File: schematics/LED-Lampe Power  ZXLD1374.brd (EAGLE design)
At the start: 100 x 51.4 mm, 50 parts, among them X2 MKDSN1,5/4-5,08, X6 MKDSN1,5/2-5,08

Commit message: - finalized layout - moved to eagle 6.5
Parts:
- added C25: 220µF / 50V Pan FR, rcl:E5-10,5
- C1: value 470µ / 50V -> 220µF / 50V Pan FR; device rcl:E5-13 -> rcl:E5-10,5
- R25, R3, R9: device resistor:R1206 -> rcl:R1206
- R7, R8: device resistor:R1206@1 -> rcl:R1206
- U$1: value FASTON_PIS4728 220µH -> PIS4728 220µH
- U$2, U$3: value FASTON_PIS4728 100µH -> PIS4728 100µH
- moved C1 17.3 mm to (58.4, 19.8), turned to 270 degrees
- moved C19 15.8 mm to (43.5, 20.0), flipped to the top, turned to 0 degrees
- moved R25 15.3 mm to (40.3, 18.6), flipped to the top, turned to 90 degrees
- moved C20 10.8 mm to (43.5, 17.1), flipped to the top, turned to 0 degrees
- moved C35 4.27 mm to (54.5, 17.1), turned to 0 degrees
- moved C24 4.02 mm to (54.5, 20.0), turned to 0 degrees
- moved R7 3.90 mm to (51.1, 18.6), turned to 90 degrees
- moved C11 2.70 mm to (35.7, 33.2), flipped to the bottom
- moved C2 1.11 mm to (32.9, 22.9)
- moved C32 1.11 mm to (32.9, 19.7)
- moved R3 1.11 mm to (36.0, 21.3)
- moved C13 0.48 mm to (22.4, 33.7)
- moved C6 0.16 mm to (24.6, 32.4)
- moved U$5 0.05 mm to (62.5, 42.5)
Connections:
- net +24V: no longer C1.+
- net GND: now also C25.-
- net N$48: now also C25.+
- net N$7: now also C1.+
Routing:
- net N$48: track 9.02 -> 22.8 mm
- net N$6: track 91.0 -> 81.8 mm
- net +24V: track 53.3 -> 45.7 mm
- net N$7: track 17.3 -> 21.1 mm
- net N$12: track 51.5 -> 49.2 mm
- net N$1: track 26.6 -> 24.3 mm

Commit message: - fix ZXLD1374 case
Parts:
- removed U$1: PIS4728 220µH, LED-Treiber:FASTON_PIS4728
- removed U$2: PIS4728 100µH, LED-Treiber:FASTON_PIS4728
- added L$1: PIS4728 220µH, LED-Treiber:FASTON_PIS4728
- added L$2: PIS4728 100µH, LED-Treiber:FASTON_PIS4728
- U$5, U$6: device ZXLD:TSSOP20CA(FE) -> ZXLD:TSSOP20
- moved R15 7.28 mm to (62.7, 41.5), flipped to the top
- moved C17 6.26 mm to (63.3, 38.4)
- moved C14 5.48 mm to (58.1, 46.8)
- moved U$5 4.67 mm to (57.9, 41.6)
- moved C9 4.13 mm to (69.8, 33.0)
- moved D2 4.13 mm to (55.2, 31.8)
- moved C10 4.13 mm to (61.6, 31.8)
- moved C15 4.13 mm to (61.6, 34.0)
- moved C18 4.13 mm to (61.6, 29.5)
- moved R9 4.13 mm to (61.6, 34.0)
- moved C16 3.24 mm to (66.3, 12.5), turned to 270 degrees
- moved R8 2.81 mm to (70.2, 16.4)
- moved C5 2.01 mm to (20.0, 33.3), flipped to the bottom
- moved C21 1.83 mm to (70.9, 4.06)
- moved U$6 0.57 mm to (71.0, 9.21)
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- renumbered U$3 to L$3
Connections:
- net +3V3: now also L$1.P$2; no longer U$1.P$2
- net N$12: now also L$2.P$2; no longer U$2.P$2
- net N$17: now also L$2.P$1; no longer U$2.P$1
- net N$5: now also L$1.P$1; no longer U$1.P$1
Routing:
- net P1.6: track 88.0 -> 80.0 mm, vias 1 -> 0
- net N$15: track 35.3 -> 40.3 mm
- net N$21: track 11.4 -> 7.14 mm, vias 2 -> 0
- net N$2: track 11.4 -> 7.14 mm, vias 2 -> 0
- net N$12: track 49.2 -> 53.4 mm
- net +3V3: track 51.1 -> 47.1 mm
- net N$48: track 22.8 -> 18.9 mm
- net N$13: track 9.00 -> 6.85 mm, vias 1 -> 0
- net N$6: track 81.8 -> 79.8 mm
- net N$5: track 11.0 -> 9.23 mm
- net N$23: track 16.6 -> 18.3 mm
- net N$18: track 7.66 -> 9.07 mm
- net N$20: track 35.7 -> 36.9 mm
- net N$22: track 2.78 -> 2.24 mm
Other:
- board text added: "Control"
- board text added: "LED 1 + -"
- board text added: "LED 2 + -"
- board text added: "Power in + -"

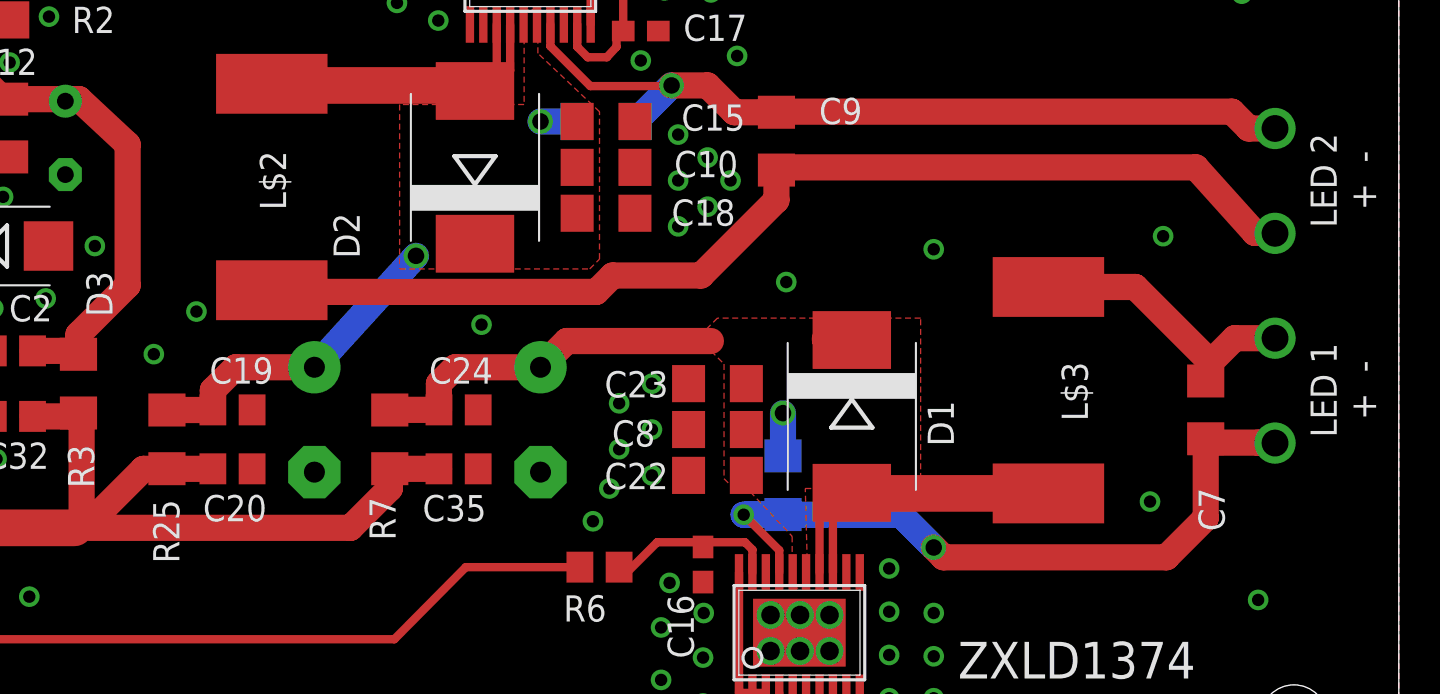
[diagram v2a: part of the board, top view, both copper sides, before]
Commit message: 
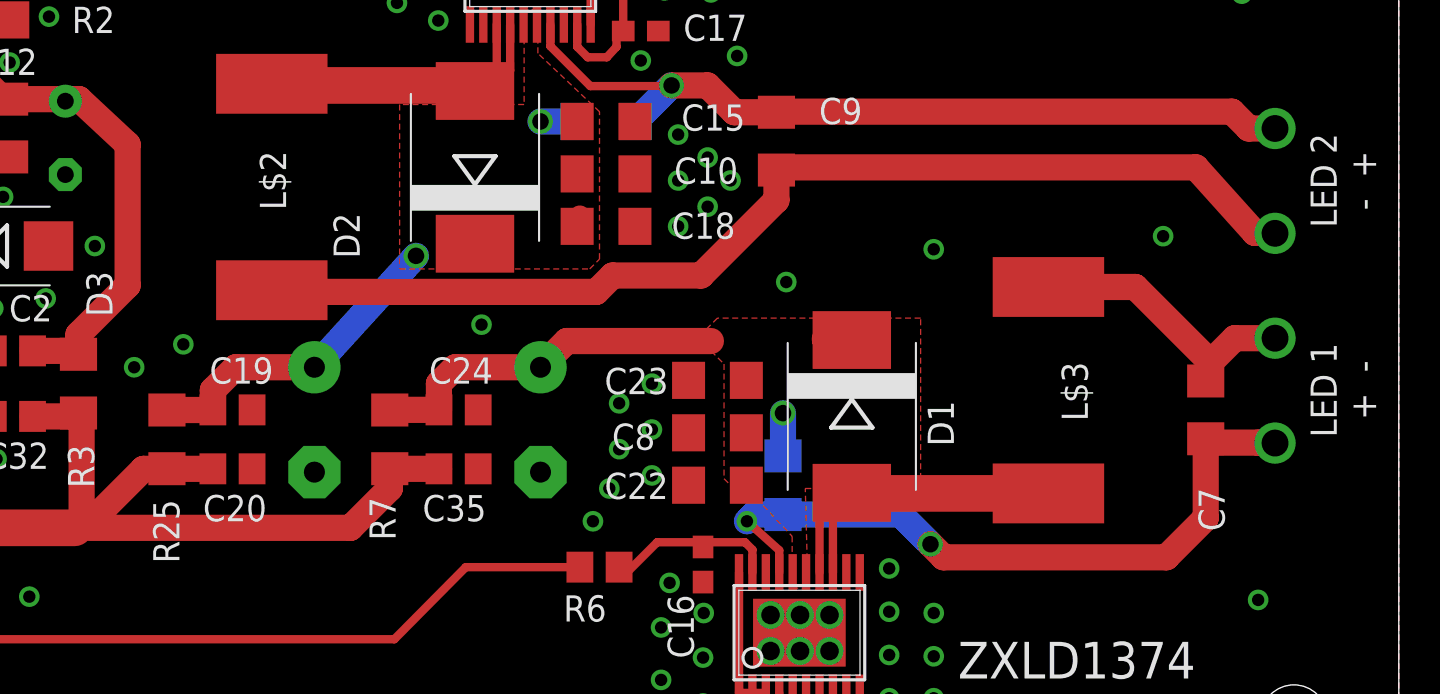
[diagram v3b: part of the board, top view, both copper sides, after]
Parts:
- moved C18 0.64 mm to (61.6, 28.9)
- moved C22 0.48 mm to (67.0, 16.4)
- moved C10 0.32 mm to (61.6, 31.4)
- moved C8 0.16 mm to (67.0, 18.9)
- moved C23 0.16 mm to (67.0, 21.4)
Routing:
- net N$20: track 36.9 -> 34.6 mm
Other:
- board text added: "LED 2 - +"
- board text removed: "LED 2 + -"
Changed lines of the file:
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@@
 <layer number="19" name="Unrouted" color="6" fill="1" visible="yes" active="yes"/>
 <layer number="20" name="Dimension" color="15" fill="1" visible="yes" active="yes"/>
-<layer number="21" name="tPlace" color="7" fill="1" visible="yes" active="yes"/>
-<layer number="22" name="bPlace" color="7" fill="1" visible="yes" active="yes"/>
+<layer number="21" name="tPlace" color="7" fill="1" visible="no" active="yes"/>
+<layer number="22" name="bPlace" color="7" fill="1" visible="no" active="yes"/>
 <layer number="23" name="tOrigins" color="15" fill="1" visible="yes" active="yes"/>
 <layer number="24" name="bOrigins" color="15" fill="1" visible="yes" active="yes"/>
-<layer number="25" name="tNames" color="7" fill="1" visible="yes" active="yes"/>
-<layer number="26" name="bNames" color="7" fill="1" visible="yes" active="yes"/>
-<layer number="27" name="tValues" color="7" fill="1" visible="yes" active="yes"/>
-<layer number="28" name="bValues" color="7" fill="1" visible="yes" active="yes"/>
+<layer number="25" name="tNames" color="7" fill="1" visible="no" active="yes"/>
+<layer number="26" name="bNames" color="7" fill="1" visible="no" active="yes"/>
+<layer number="27" name="tValues" color="7" fill="1" visible="no" active="yes"/>
+<layer number="28" name="bValues" color="7" fill="1" visible="no" active="yes"/>
 <layer number="29" name="tStop" color="7" fill="3" visible="yes" active="yes"/>
 <layer number="30" name="bStop" color="7" fill="6" visible="yes" active="yes"/>
@@
 +  -</text>
 <text x="97.31375" y="31.115" size="1.27" layer="25" rot="R90" align="center">LED 2
-+  -</text>
+-  +</text>
 <text x="4.60375" y="20.0025" size="1.27" layer="25" rot="R270" align="center">Power in
 +  -</text>
 <text x="8.41375" y="34.6075" size="1.27" layer="25" rot="R180" align="center">Control</text>
+<rectangle x1="76.835" y1="14.9225" x2="89.2175" y2="26.9875" layer="41"/>
+<rectangle x1="39.21125" y1="24.765" x2="51.59375" y2="36.83" layer="41"/>
+<rectangle x1="16.03375" y1="18.415" x2="28.41625" y2="30.48" layer="41"/>
 </plain>
 <attributes>
@@
 <attribute name="VALUE" x="71.91375" y="32.03575" size="1.27" layer="27"/>
 </element>
-<element name="C10" library="resistor" package="C1206" value="2,2µF / 50V X7R" x="61.595" y="31.75" smashed="yes">
-<attribute name="NAME" x="64.897" y="31.27375" size="1.27" layer="25"/>
-<attribute name="VALUE" x="68.453" y="28.8925" size="1.27" layer="27"/>
+<element name="C10" library="resistor" package="C1206" value="2,2µF / 50V X7R" x="61.595" y="31.4325" smashed="yes">
+<attribute name="NAME" x="64.897" y="30.95625" size="1.27" layer="25"/>
+<attribute name="VALUE" x="68.453" y="28.575" size="1.27" layer="27"/>
 </element>
 <element name="L$2" library="LED-Treiber" package="FASTON_PIS4728" value="PIS4728 100µH" x="45.4025" y="30.7975" smashed="yes">
@@
 <attribute name="VALUE" x="65.56375" y="35.52825" size="1.27" layer="27"/>
 </element>
-<element name="C18" library="resistor" package="C1206" value="2,2µF / 50V X7R" x="61.595" y="29.5275" smashed="yes">
-<attribute name="NAME" x="64.77" y="28.92425" size="1.27" layer="25"/>
-<attribute name="VALUE" x="61.9125" y="26.95575" size="1.27" layer="27"/>
+<element name="C18" library="resistor" package="C1206" value="2,2µF / 50V X7R" x="61.595" y="28.8925" smashed="yes">
+<attribute name="NAME" x="64.77" y="28.28925" size="1.27" layer="25"/>
+<attribute name="VALUE" x="61.9125" y="26.32075" size="1.27" layer="27"/>
 </element>
 <element name="C19" library="rcl" package="C0805" value="10n" x="43.4975" y="20.0025" smashed="yes">
@@
 <attribute name="VALUE" x="93.218" y="14.12875" size="1.27" layer="27" rot="R90"/>
 </element>
-<element name="C8" library="resistor" package="C1206" value="2,2µF / 50V X7R" x="66.9925" y="19.05" smashed="yes" rot="R180">
-<attribute name="NAME" x="63.97625" y="19.4945" size="1.27" layer="25" rot="R180"/>
-<attribute name="VALUE" x="67.15125" y="26.543" size="1.27" layer="27" rot="R180"/>
+<element name="C8" library="resistor" package="C1206" value="2,2µF / 50V X7R" x="66.9925" y="18.89125" smashed="yes" rot="R180">
+<attribute name="NAME" x="63.97625" y="19.33575" size="1.27" layer="25" rot="R180"/>
+<attribute name="VALUE" x="67.15125" y="26.38425" size="1.27" layer="27" rot="R180"/>
 </element>
 <element name="L$3" library="LED-Treiber" package="FASTON_PIS4728" value="PIS4728 100µH" x="83.02625" y="20.955" smashed="yes" rot="R180">
@@
 <attribute name="VALUE" x="79.91475" y="3.429" size="1.27" layer="27"/>
 </element>
-<element name="C22" library="resistor" package="C1206" value="1µF / 50V X7R" x="66.9925" y="16.8275" smashed="yes" rot="R180">
-<attribute name="NAME" x="64.61125" y="17.43075" size="1.27" layer="25" rot="R180"/>
-<attribute name="VALUE" x="71.27875" y="23.52675" size="1.27" layer="27" rot="R180"/>
-</element>
-<element name="C23" library="resistor" package="C1206" value="2,2µF / 50V X7R" x="66.9925" y="21.2725" smashed="yes" rot="R180">
-<attribute name="NAME" x="64.61125" y="21.87575" size="1.27" layer="25" rot="R180"/>
-<attribute name="VALUE" x="71.27875" y="25.11425" size="1.27" layer="27" rot="R180"/>
+<element name="C22" library="resistor" package="C1206" value="1µF / 50V X7R" x="66.9925" y="16.35125" smashed="yes" rot="R180">
+<attribute name="NAME" x="64.61125" y="16.9545" size="1.27" layer="25" rot="R180"/>
+<attribute name="VALUE" x="71.27875" y="23.0505" size="1.27" layer="27" rot="R180"/>
+</element>
+<element name="C23" library="resistor" package="C1206" value="2,2µF / 50V X7R" x="66.9925" y="21.43125" smashed="yes" rot="R180">
+<attribute name="NAME" x="64.61125" y="22.0345" size="1.27" layer="25" rot="R180"/>
+<attribute name="VALUE" x="71.27875" y="25.273" size="1.27" layer="27" rot="R180"/>
 </element>
 <element name="C24" library="rcl" package="C0805" value="10n" x="54.45125" y="20.0025" smashed="yes">
@@
 <via x="65.0875" y="33.3375" extent="1-16" drill="0.6"/>
 <via x="55.5625" y="24.13" extent="1-16" drill="0.6"/>
-<via x="87.9475" y="15.5575" extent="1-16" drill="0.6"/>
 <via x="53.467" y="38.862" extent="1-16" drill="0.6"/>
 <via x="63.754" y="47.0535" extent="1-16" drill="0.6"/>
@@
 <contactref element="C1" pad="-"/>
 <contactref element="C25" pad="-"/>
-<via x="41.75125" y="24.765" extent="1-16" drill="0.6"/>
-<via x="39.6875" y="22.70125" extent="1-16" drill="0.6"/>
+<via x="41.11625" y="23.1775" extent="1-16" drill="0.6"/>
+<via x="38.735" y="22.06625" extent="1-16" drill="0.6"/>
 <via x="53.467" y="41.11625" extent="1-16" drill="0.6"/>
 <via x="51.46675" y="44.3865" extent="1-16" drill="0.6"/>
@@
 <wire x1="55.88" y1="27.415" x2="55.245" y2="28.05" width="1.016" layer="1"/>
 <via x="52.3875" y="27.46375" extent="1-16" drill="0.8"/>
-<wire x1="60.325" y1="29.3975" x2="60.195" y2="29.5275" width="1.016" layer="1"/>
+<wire x1="60.325" y1="29.3975" x2="60.195" y2="28.8925" width="1.016" layer="1"/>
 <wire x1="52.23125" y1="27.46625" x2="52.3875" y2="27.46375" width="1.016" layer="16"/>
 <via x="58.42" y="33.9725" extent="1-16" drill="0.8"/>
@@
 <contactref element="U$6" pad="17"/>
 <contactref element="C7" pad="1"/>
-<via x="68.2625" y="14.9225" extent="1-16" drill="0.6"/>
-<wire x1="68.2625" y1="14.9225" x2="70.1675" y2="14.92925" width="1.27" layer="16"/>
+<via x="68.42125" y="14.605" extent="1-16" drill="0.6"/>
 <wire x1="90.64625" y1="18.6025" x2="90.64625" y2="14.76375" width="1.27" layer="1"/>
 <wire x1="90.64625" y1="14.76375" x2="88.74125" y2="12.85875" width="1.27" layer="1"/>
 <wire x1="88.74125" y1="12.85875" x2="77.94625" y2="12.85875" width="1.27" layer="1"/>
-<wire x1="77.94625" y1="12.85875" x2="77.47" y2="13.335" width="1.27" layer="1"/>
-<via x="77.47" y="13.335" extent="1-16" drill="0.8"/>
-<wire x1="77.47" y1="13.335" x2="75.8825" y2="14.9225" width="1.27" layer="16"/>
-<wire x1="75.8825" y1="14.9225" x2="68.2625" y2="14.9225" width="1.27" layer="16"/>
+<wire x1="77.94625" y1="12.85875" x2="77.31125" y2="13.49375" width="1.27" layer="1"/>
+<via x="77.31125" y="13.49375" extent="1-16" drill="0.8"/>
 <contactref element="X2" pad="1"/>
 <wire x1="94.005" y1="18.3939" x2="93.80015" y2="18.3939" width="1.016" layer="1"/>
@@
 <contactref element="R8" pad="2"/>
 <wire x1="69.98625" y1="12.1253" x2="69.98625" y2="13.19875" width="0.4064" layer="1"/>
-<wire x1="69.98625" y1="13.19875" x2="68.2625" y2="14.9225" width="0.4064" layer="1"/>
+<wire x1="69.98625" y1="13.19875" x2="68.42125" y2="14.605" width="0.4064" layer="1"/>
+<wire x1="70.1675" y1="14.92925" x2="75.87575" y2="14.92925" width="1.27" layer="16"/>
+<wire x1="75.87575" y1="14.92925" x2="77.31125" y2="13.49375" width="1.27" layer="16"/>
+<wire x1="70.1675" y1="14.92925" x2="68.7455" y2="14.92925" width="1.27" layer="16"/>
+<wire x1="68.7455" y1="14.92925" x2="68.42125" y2="14.605" width="1.27" layer="16"/>
 </signal>
 <signal name="N$21">
@@
 </signal>
 </signals>
+<errors>
+</errors>
 </board>
 </drawing>
